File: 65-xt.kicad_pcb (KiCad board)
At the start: 2 copper layers, 346.7 x 94.3 mm, 179 parts, among them J1 Conn_01x04, Q1 2N7002, SW1 SW_Push, U1 MCP1700-3302E_SOT23, U2 STM32F072CBT6

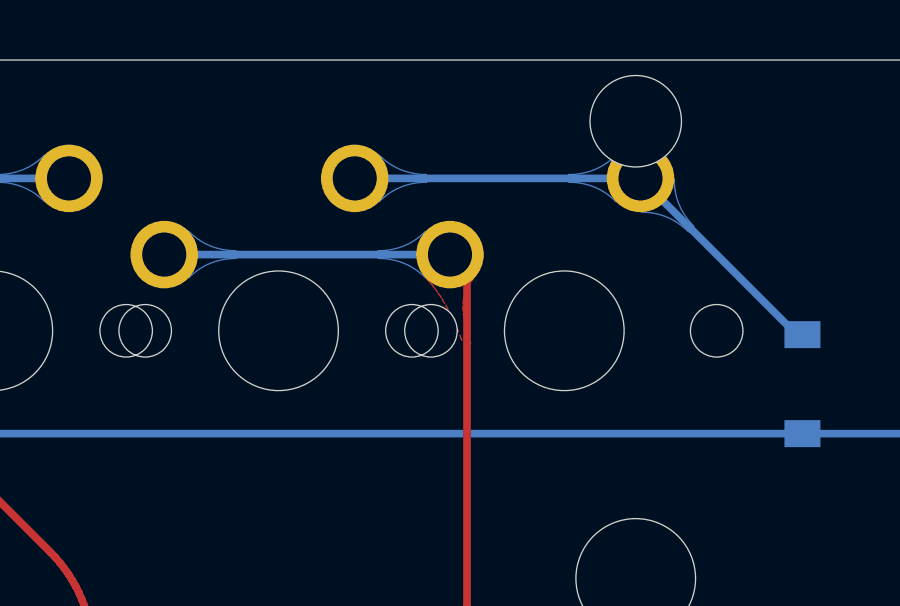
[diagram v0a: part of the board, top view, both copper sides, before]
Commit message: updating reset/boot R and C values
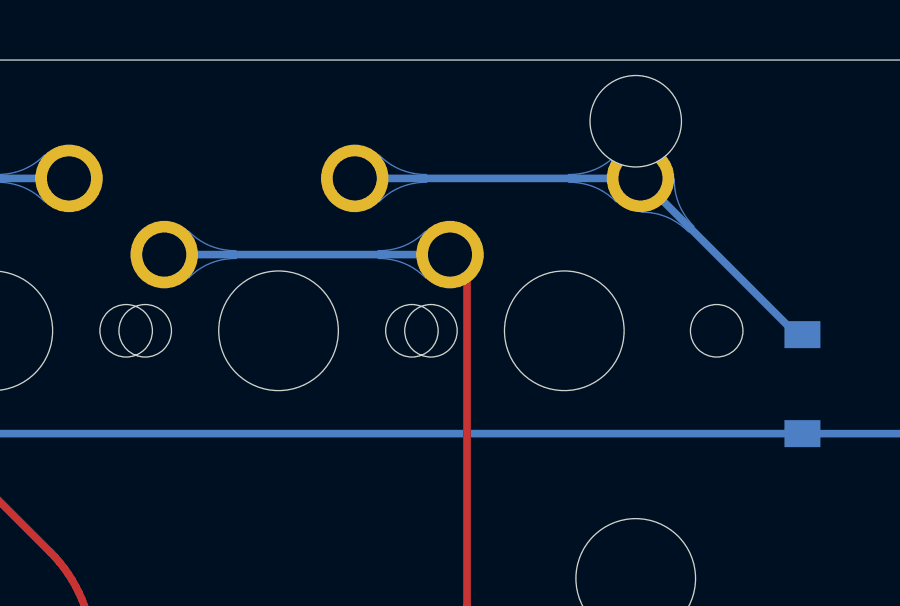
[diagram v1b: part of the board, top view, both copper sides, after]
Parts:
- C3: value 1uF -> 4.7uF
- C4: value 1uF -> 470nF
- R2: value 100k -> 10k
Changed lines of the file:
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@@
       (effects (font (size 1 1) (thickness 0.15)) (justify mirror))
     )
-    (fp_text value 100k (at 0 -1.43 90) (layer B.Fab)
+    (fp_text value 10k (at 0 -1.43 90) (layer B.Fab)
       (effects (font (size 1 1) (thickness 0.15)) (justify mirror))
     )
@@
       (effects (font (size 1 1) (thickness 0.15)) (justify mirror))
     )
-    (fp_text value 1uF (at 0 -1.43 90) (layer B.Fab)
+    (fp_text value 470nF (at 0 -1.43 90) (layer B.Fab)
       (effects (font (size 1 1) (thickness 0.15)) (justify mirror))
     )
@@
       (effects (font (size 1 1) (thickness 0.15)) (justify mirror))
     )
-    (fp_text value 1uF (at 0 -1.43 90) (layer B.Fab)
+    (fp_text value 4.7uF (at 0 -1.43 90) (layer B.Fab)
       (effects (font (size 1 1) (thickness 0.15)) (justify mirror))
     )
@@
       )
     )
-  )
-  (zone (net 107) (net_name Col16) (layer F.Cu) (hatch edge 0.508)
-    (priority 16962)
-    (connect_pads yes (clearance 0.2))
-    (min_thickness 0.0254)
-    (fill yes (arc_segments 32) (thermal_gap 0.508) (thermal_bridge_width 0.508))
-    (polygon
-      (pts
-        (xy 450.909001 168.711372) (xy 450.807875 168.415044) (xy 450.7313 168.13628) (xy 450.679275 167.875077) (xy 450.6518 167.631437)
-        (xy 450.648875 167.40536) (xy 450.6705 167.196845) (xy 450.716675 167.005892) (xy 450.7874 166.832502) (xy 450.882675 166.676675)
-        (xy 451.0025 166.53841) (xy 450.215 165.1725) (xy 449.4275 166.53841) (xy 449.558665 166.676675) (xy 449.68796 166.832502)
-        (xy 449.815385 167.005892) (xy 449.94094 167.196845) (xy 450.064625 167.40536) (xy 450.18644 167.631437) (xy 450.306385 167.875077)
-        (xy 450.42446 168.13628) (xy 450.540665 168.415044) (xy 450.655001 168.711372)
-      )
-    )
